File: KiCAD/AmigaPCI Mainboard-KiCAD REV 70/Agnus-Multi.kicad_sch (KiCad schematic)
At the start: 13 parts, among them J203 RAMEN, J206 CLK/VBB, U202 Agnus_MULTI, U229 74CBT16233

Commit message: Add JLCPCB part numbers and fix 74LVC244 footprints.
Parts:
- AGNUS1: LCSC (none) -> C124384
- C213, C257, C267: LCSC (none) -> C14663
- J206: LCSC (none) -> C49257
- R203, R223, R229: LCSC (none) -> C25804
- R222, R238: LCSC (none) -> C23182
- U202: LCSC (none) -> C5445002
- U229: LCSC (none) -> C2674759
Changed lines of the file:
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@@
 	(title_block
 		(title "AMIGA PCI")
-		(date "2026-04-16")
+		(date "2026-04-23")
 		(rev "7.0")
 	)
@@
 			)
 		)
+		(property "LCSC" "C23182"
+			(at 375.92 31.75 0)
+			(effects
+				(font
+					(size 1.27 1.27)
+				)
+				(hide yes)
+			)
+		)
 		(pin "1"
 		)
@@
 			)
 		)
+		(property "LCSC" "C2674759"
+			(at 166.37 100.33 0)
+			(effects
+				(font
+					(size 1.27 1.27)
+				)
+				(hide yes)
+			)
+		)
 		(pin "1"
 		)
@@
 			)
 		)
+		(property "LCSC" "C2674759"
+			(at 281.94 50.8 0)
+			(effects
+				(font
+					(size 1.27 1.27)
+				)
+				(hide yes)
+			)
+		)
 		(pin "1"
 		)
@@
 			)
 		)
+		(property "LCSC" "C5445002"
+			(at 52.07 243.84 0)
+			(effects
+				(font
+					(size 1.27 1.27)
+				)
+				(hide yes)
+			)
+		)
 		(pin "1"
 		)
@@
 			)
 		)
+		(property "LCSC" "C2674759"
+			(at 279.4 167.64 0)
+			(effects
+				(font
+					(size 1.27 1.27)
+				)
+				(hide yes)
+			)
+		)
 		(pin "1"
 		)
@@
 			)
 		)
+		(property "LCSC" "C49257"
+			(at 303.53 62.23 0)
+			(effects
+				(font
+					(size 1.27 1.27)
+				)
+				(hide yes)
+			)
+		)
 		(pin "1"
 		)
@@
 			)
 		)
+		(property "LCSC" "C25804"
+			(at 226.06 43.18 0)
+			(effects
+				(font
+					(size 1.27 1.27)
+				)
+				(hide yes)
+			)
+		)
 		(pin "1"
 		)
@@
 			)
 		)
+		(property "LCSC" "C2674759"
+			(at 281.94 92.71 0)
+			(effects
+				(font
+					(size 1.27 1.27)
+				)
+				(hide yes)
+			)
+		)
 		(pin "1"
 		)
@@
 			)
 		)
+		(property "LCSC" "C2674759"
+			(at 163.83 170.18 0)
+			(effects
+				(font
+					(size 1.27 1.27)
+				)
+				(hide yes)
+			)
+		)
 		(pin "1"
 		)
@@
 			)
 		)
+		(property "LCSC" ""
+			(at 76.2 60.96 0)
+			(effects
+				(font
+					(size 1.27 1.27)
+				)
+				(hide yes)
+			)
+		)
 		(pin "1"
 		)
@@
 			)
 		)
+		(property "LCSC" "C2674759"
+			(at 163.83 152.4 0)
+			(effects
+				(font
+					(size 1.27 1.27)
+				)
+				(hide yes)
+			)
+		)
 		(pin "1"
 		)
@@
 			)
 		)
+		(property "LCSC" "C2674759"
+			(at 269.24 251.46 0)
+			(effects
+				(font
+					(size 1.27 1.27)
+				)
+				(hide yes)
+			)
+		)
 		(pin "1"
 		)
@@
 			)
 		)
+		(property "LCSC" "C25804"
+			(at 232.41 228.6 0)
+			(effects
+				(font
+					(size 1.27 1.27)
+				)
+				(hide yes)
+			)
+		)
 		(pin "1"
 		)
@@
 			)
 		)
+		(property "LCSC" "C14663"
+			(at 63.5 243.84 0)
+			(effects
+				(font
+					(size 1.27 1.27)
+				)
+				(hide yes)
+			)
+		)
 		(pin "1"
 		)
@@
 			)
 		)
+		(property "LCSC" "C2674759"
+			(at 356.87 115.57 0)
+			(effects
+				(font
+					(size 1.27 1.27)
+				)
+				(hide yes)
+			)
+		)
 		(pin "1"
 		)
@@
 			)
 		)
+		(property "LCSC" "C2674759"
+			(at 330.2 62.23 0)
+			(effects
+				(font
+					(size 1.27 1.27)
+				)
+				(hide yes)
+			)
+		)
 		(pin "1"
 		)
@@
 			)
 		)
+		(property "LCSC" "C2674759"
+			(at 281.94 77.47 0)
+			(effects
+				(font
+					(size 1.27 1.27)
+				)
+				(hide yes)
+			)
+		)
 		(pin "1"
 		)
@@
 			)
 		)
+		(property "LCSC" "C23182"
+			(at 375.92 36.83 0)
+			(effects
+				(font
+					(size 1.27 1.27)
+				)
+				(hide yes)
+			)
+		)
 		(pin "1"
 		)
@@
 			)
 		)
+		(property "LCSC" "C2674759"
+			(at 279.4 181.61 0)
+			(effects
+				(font
+					(size 1.27 1.27)
+				)
+				(hide yes)
+			)
+		)
 		(pin "1"
 		)
@@
 			)
 		)
+		(property "LCSC" "C124384"
+			(at 209.55 246.38 0)
+			(effects
+				(font
+					(size 1.27 1.27)
+				)
+				(hide yes)
+			)
+		)
 		(pin "1"
 		)
@@
 			)
 		)
+		(property "LCSC" "C2674759"
+			(at 281.94 36.83 0)
+			(effects
+				(font
+					(size 1.27 1.27)
+				)
+				(hide yes)
+			)
+		)
 		(pin "1"
 		)
@@
 			)
 		)
+		(property "LCSC" "C5445002"
+			(at 231.14 125.73 0)
+			(effects
+				(font
+					(size 1.27 1.27)
+				)
+				(hide yes)
+			)
+		)
 		(pin "1"
 		)
@@
 			)
 		)
+		(property "LCSC" "C14663"
+			(at 179.07 233.68 0)
+			(effects
+				(font
+					(size 1.27 1.27)
+				)
+				(hide yes)
+			)
+		)
 		(pin "1"
 		)
@@
 			)
 		)
+		(property "LCSC" "C14663"
+			(at 297.18 64.77 0)
+			(effects
+				(font
+					(size 1.27 1.27)
+				)
+				(hide yes)
+			)
+		)
 		(pin "1"
 		)
@@
 			)
 		)
+		(property "LCSC" "C2674759"
+			(at 163.83 245.11 0)
+			(effects
+				(font
+					(size 1.27 1.27)
+				)
+				(hide yes)
+			)
+		)
 		(pin "1"
 		)
@@
 			(at 144.78 234.95 0)
 			(effects
+				(font
+					(size 1.27 1.27)
+				)
+				(hide yes)
+			)
+		)
+		(property "LCSC" "C25804"
+			(at 144.78 234.95 0)
+			(effects

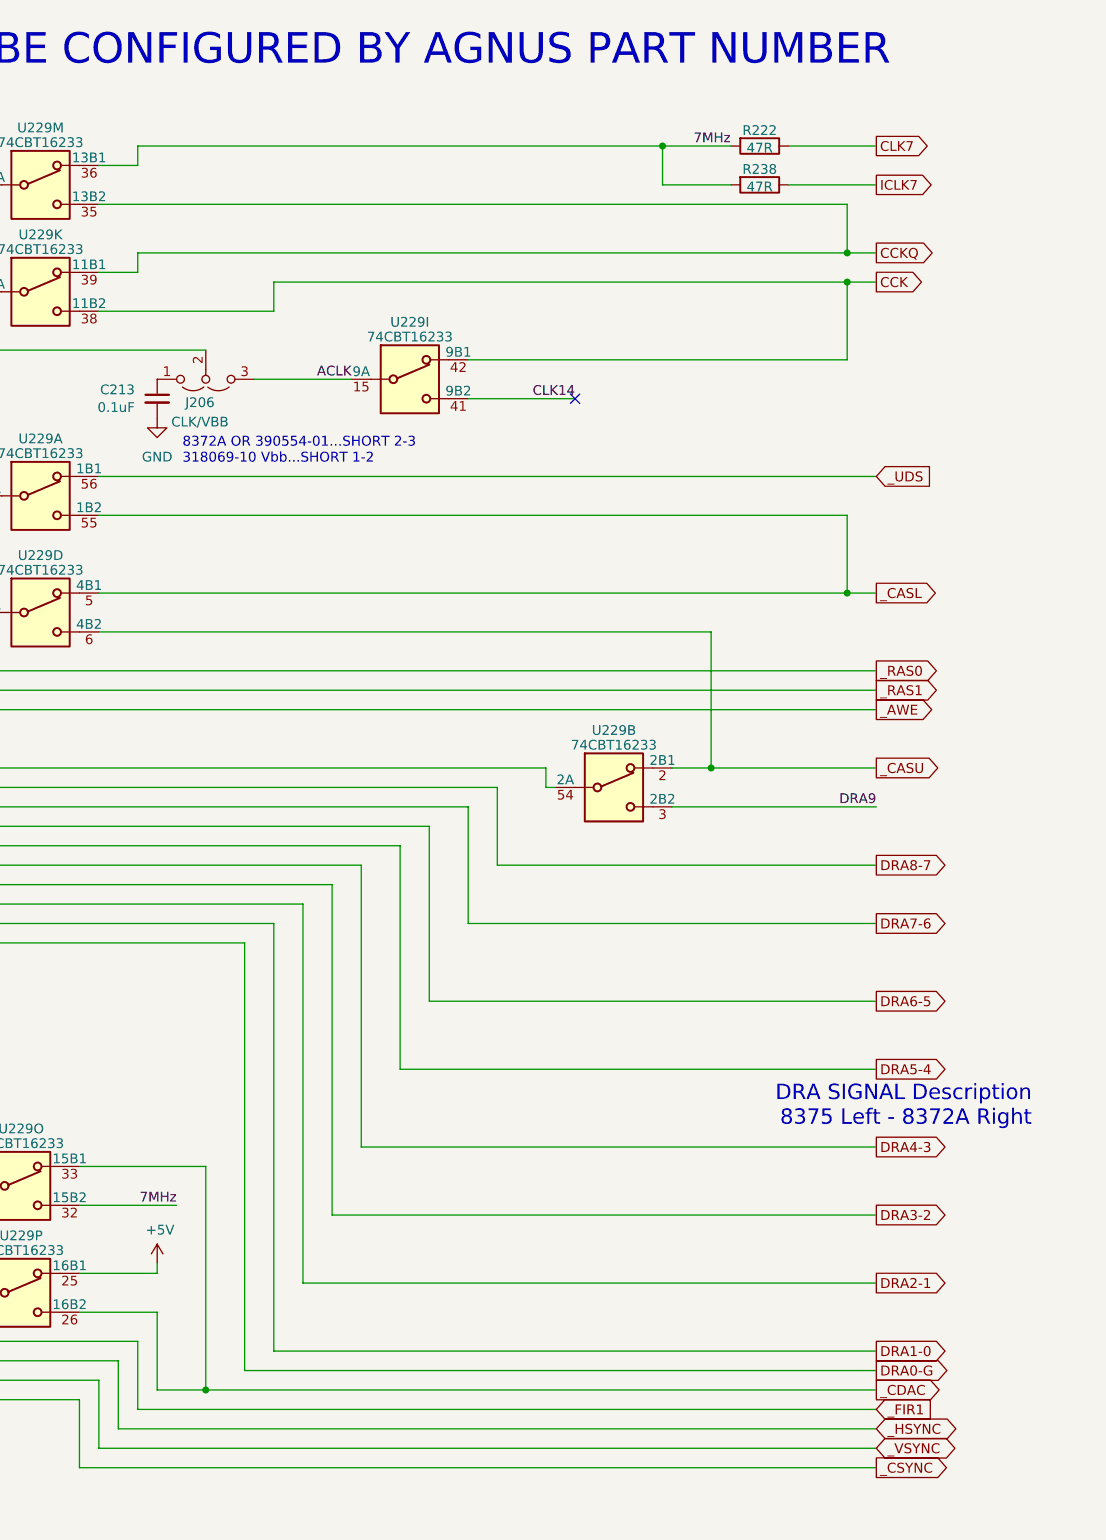
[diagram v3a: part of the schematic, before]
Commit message: Updates to revision 7 board.
Change U810 to 74LVC245 buffers
Add CDAC to U712
Add address latch to CIAs
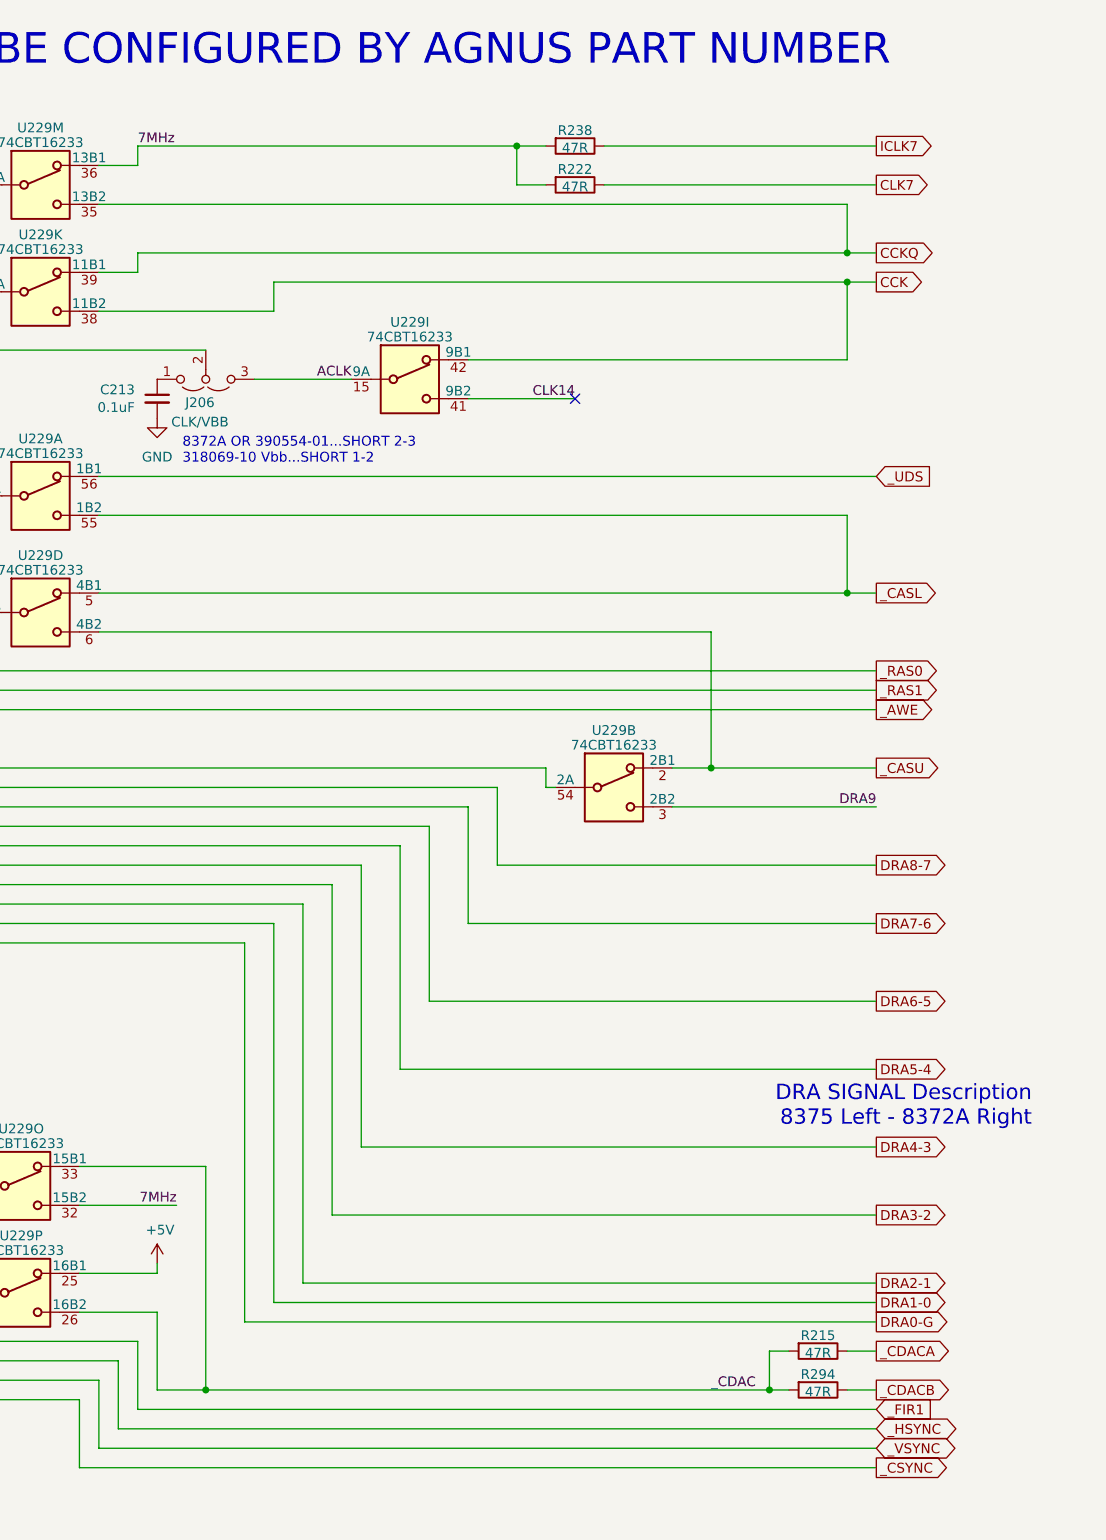
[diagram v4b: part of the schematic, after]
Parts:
- added R215, R294: 47R, Resistor_SMD:R_0603_1608Metric, symbol Device:R
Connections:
- net _CDAC: now also R215.2, R294.2
- new net _CDACA: R215.1
- new net _CDACB: R294.1
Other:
- moved on the sheet: R222, R238
